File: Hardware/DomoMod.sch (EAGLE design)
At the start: 9 parts, among them Q1 BSS138, Q2 BSS138

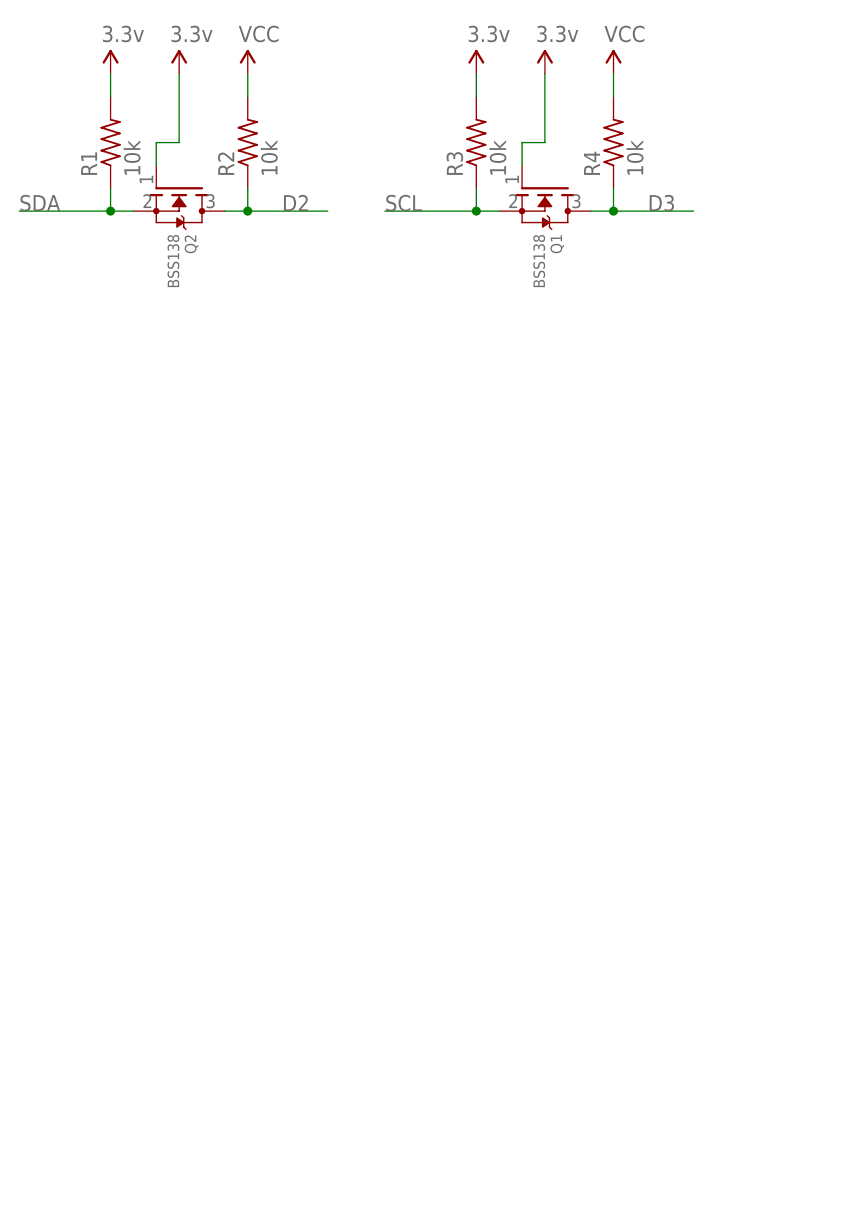
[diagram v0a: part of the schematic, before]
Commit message: Added schematics for Temp/Hum and barometric pressure sensor.
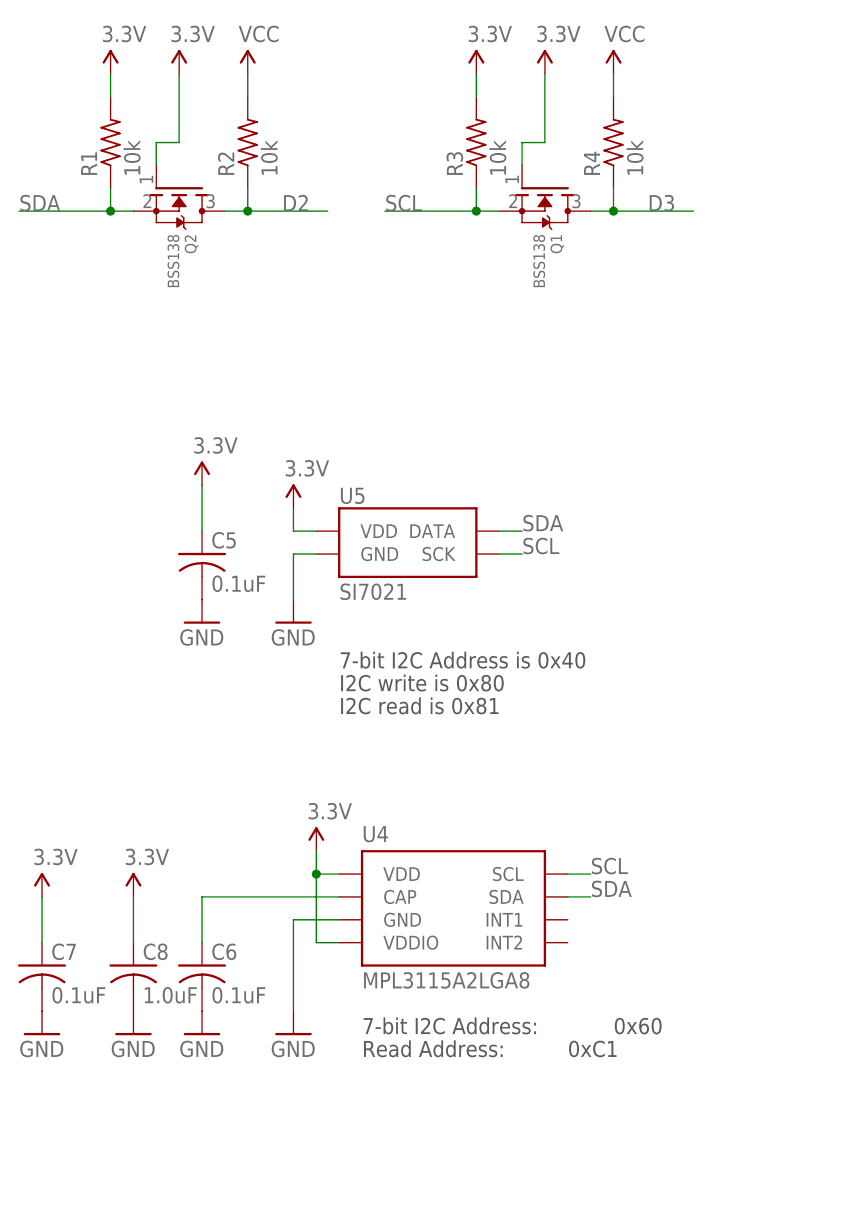
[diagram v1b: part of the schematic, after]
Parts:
- added C5, C6, C7: 0.1uF, resistor:C-USC0402
- added C8: 1.0uF, resistor:C-USC0402
- added U4: MPL3115A2LGA8, SparkFun-Sensors:MPL3115A2LGA8
- added U5: SI7021, SparkFun-Sensors:SI7021
- R1, R2, R3, R4: device resistor:R-US_R1206 -> resistor:R-US_R0402
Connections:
- new net N$5: C6.1, U4.CAP
- net 3.3V: now also C5.1, C7.1, C8.1, U4.VDD, U4.VDDIO, U5.VDD
- net GND: now also C5.2, C6.2, C7.2, C8.2, U4.GND, U5.GND
- net SCL: now also U4.SCL, U5.SCK
- net SDA: now also U4.SDA, U5.DATA
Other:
- note added: "0x60"
- note added: "0xC1"
- note added: "7-bit I2C Address is 0x40"
- note added: "7-bit I2C Address:"
- note added: "Humidity"
- note added: "I2C read is 0x81"
- note added: "I2C write is 0x80"
- note added: "Pressure"
- note added: "Read Address:"

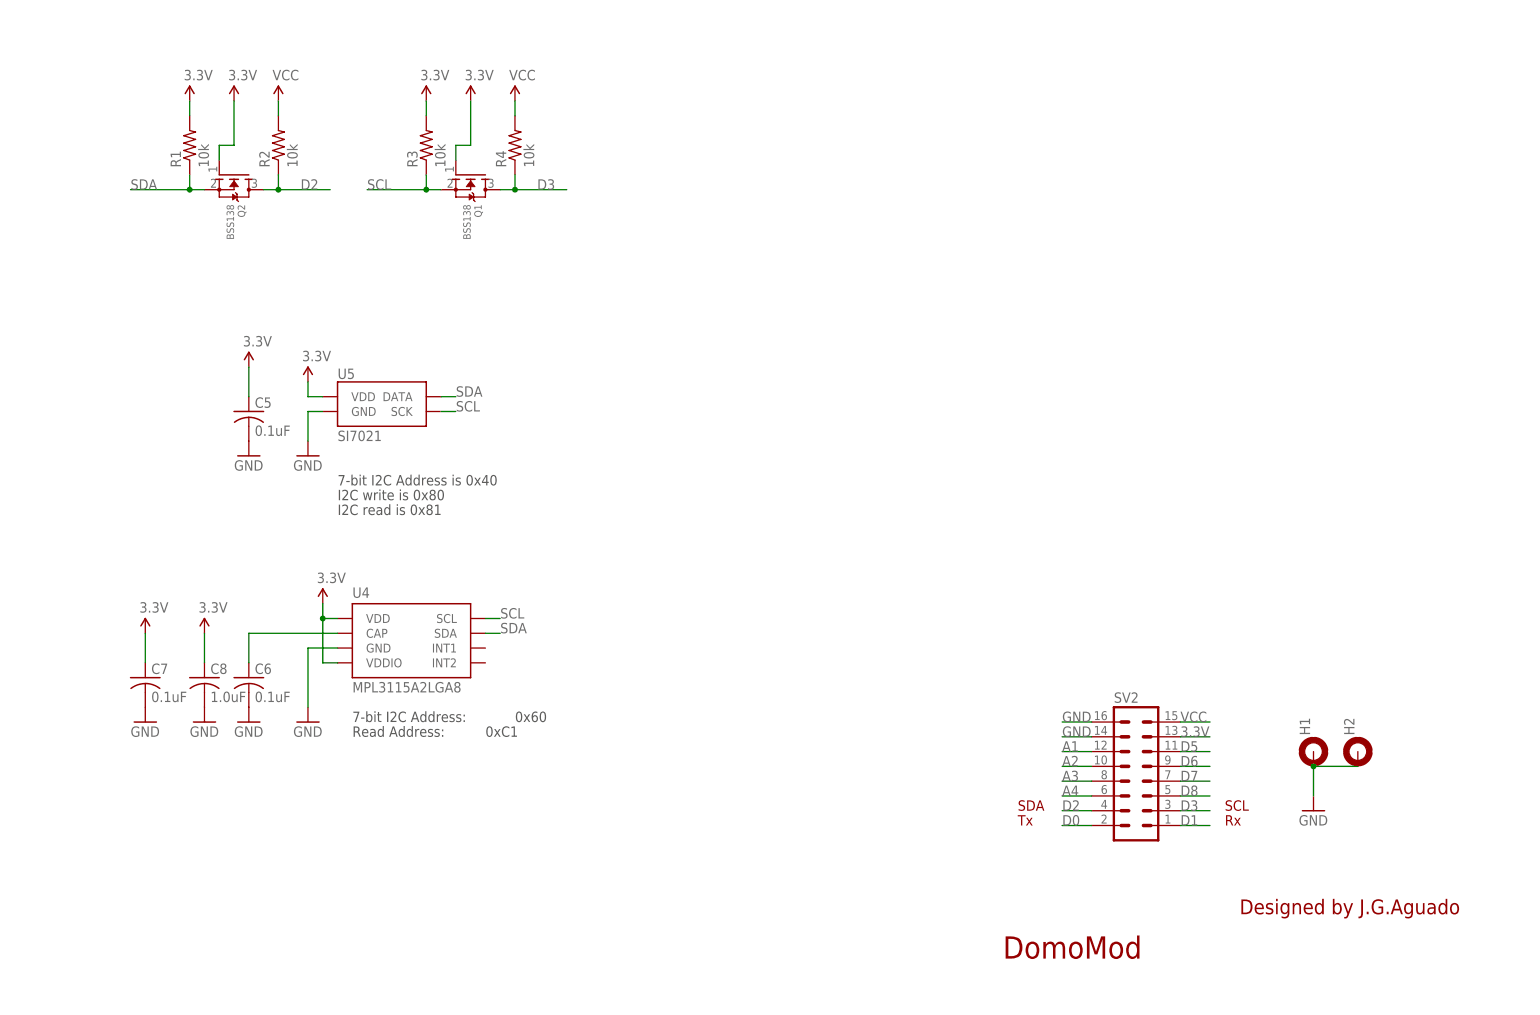
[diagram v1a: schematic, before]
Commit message: SCH: -Components placed and connected -Documented BRD: -Components placed -100% routed -DRC passed
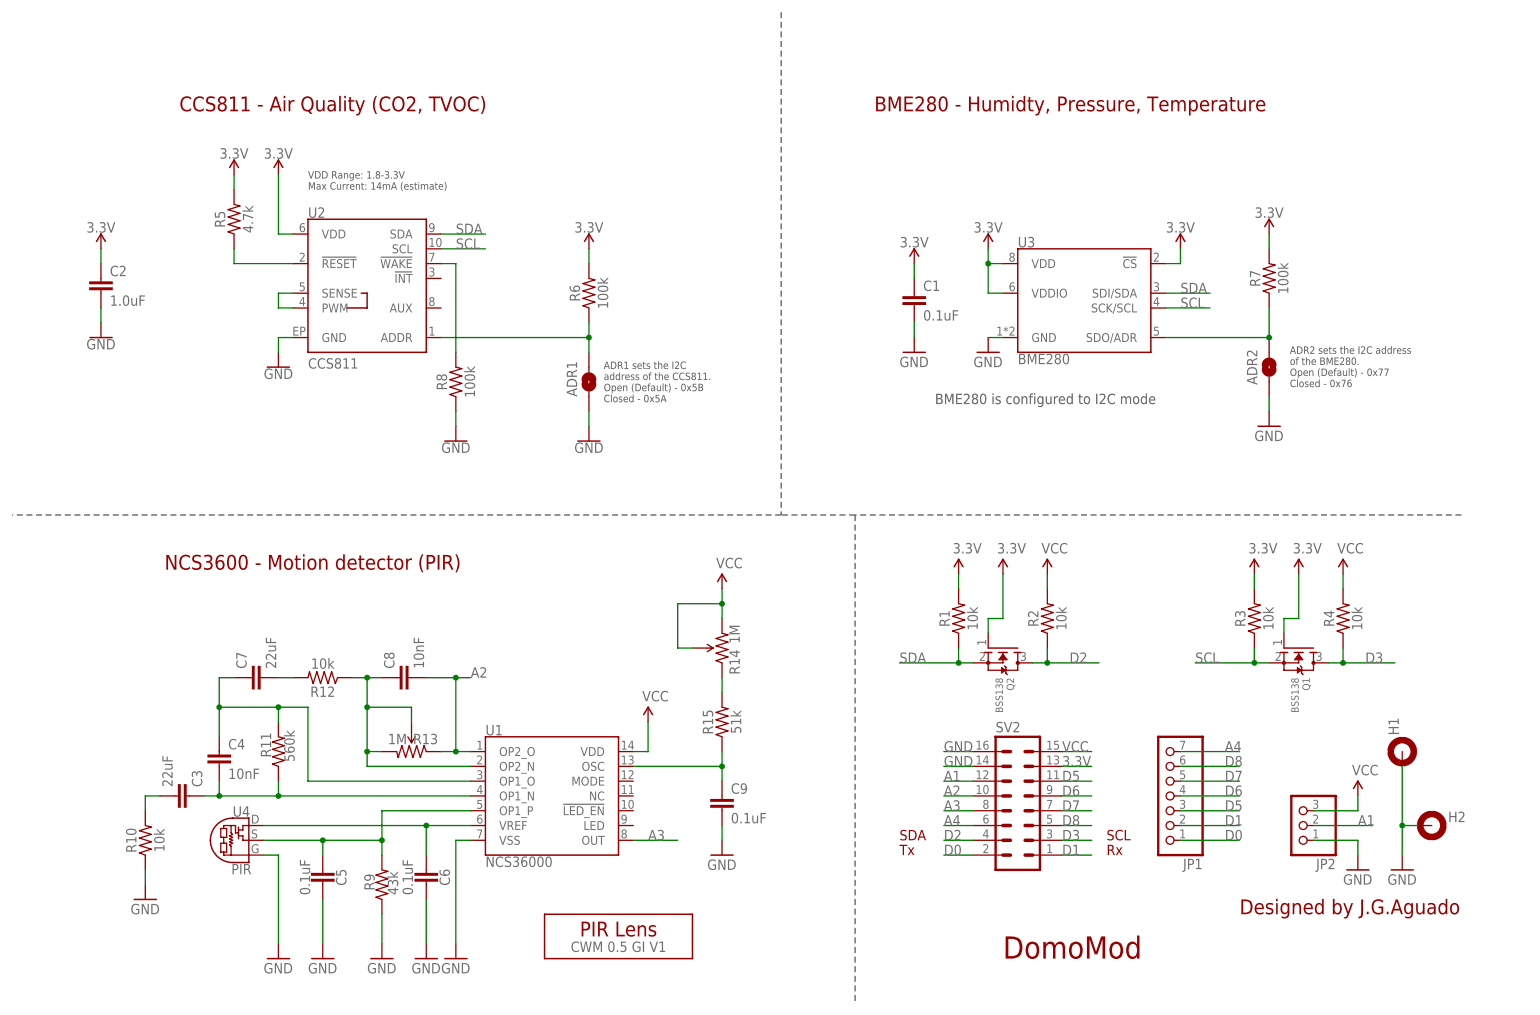
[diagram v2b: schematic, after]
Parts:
- removed U5: SI7021, SparkFun-Sensors:SI7021
- added ADR1, ADR2: JUMPER-SMT_2_NO_SILK, SparkFun-Jumpers:JUMPER-SMT_2_NO_SILK
- added C1, C9: 0.1uF, SparkFun-Capacitors:0.1UF-0603-25V-(+80/-20%)
- added C2: 1.0uF, SparkFun-Capacitors:1.0UF-0603-16V-10%
- added C3: 22uF, SparkFun-Capacitors:22UF-0805-6.3V-20%
- added C4: 10nF, SparkFun-Capacitors:10NF-0603-50V-10%
- added JP1: (no value), pinhead:PINHD-1X7/90
- added JP2: (no value), pinhead:PINHD-1X3
- added R10, R12: 10k, SparkFun-Resistors:10KOHM-0603-1/10W-1%
- added R11: 560k, openPIR-temp:560KOHM-0603-1/10W-5%
- added R13, R14: 1M, openPIR-temp:TRIMPOTTX33X-1M
- added R15: 51k, openPIR-temp:51KOHM-0603-1/10W-1%
- added R5: 4.7k, SparkFun-Resistors:4.7KOHM-0603-1/10W-1%
- added R6, R7, R8: 100k, SparkFun-Resistors:100KOHM-0603-1/10W-1%
- added R9: 43k, SparkFun-Resistors:43KOHM-0603-1/10W-1%
- added U$1: CWM 0.5 GI V1, openPIR-temp:PIR-LENSCWM-0.5-GI-V1
- added U1: NCS36000, openPIR-temp:NCS36000
- added U2: CCS811, SparkFun-Sensors:CCS811PRODUCTION
- added U3: BME280, SparkFun-Sensors:BME280
- C5, C6: device resistor:C-USC0402 -> SparkFun-Capacitors:0.1UF-0603-25V-(+80/-20%)
- C7: value 0.1uF -> 22uF; device resistor:C-USC0402 -> SparkFun-Capacitors:22UF-0805-6.3V-20%
- C8: value 1.0uF -> 10nF; device resistor:C-USC0402 -> SparkFun-Capacitors:10NF-0603-50V-10%
- R1, R2, R3, R4: device resistor:R-US_R0402 -> SparkFun-Resistors:100KOHM-0603-1/10W-1%
- U4: value MPL3115A2LGA8 -> PIR; device SparkFun-Sensors:MPL3115A2LGA8 -> openPIR-temp:PIR
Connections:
- new net !RST: R5.1, U2.!RESET!
- new net !WAKE: R8.2, U2.!WAKE!
- new net CCS811_ADDR: ADR1.2, R6.1, U2.ADDR
- new net N$1: C5.1, R9.2, U1.OP1_P, U4.S
- new net N$11: R14.CCW, R15.2
- new net N$2: C6.1, U1.VREF, U4.D
- new net N$3: C3.2, R10.2
- new net N$4: C7.2, R12.2
- new net N$6: C4.1, C7.1, R11.2, U1.OP1_O
- new net N$7: C8.1, R12.1, R13.CW, R13.WIPER, U1.OP2_N
- new net N$8: C9.1, R15.1, U1.OSC
- new net NTC_SENSE: U2.PWM, U2.SENSE
- new net SDO/ADR: ADR2.2, R7.1, U3.SDO/ADR
- net 3.3V: now also C1.1, C2.1, R5.2, R6.2, R7.2, U2.VDD, U3.!CS, U3.VDD, U3.VDDIO; no longer C5.1, C7.1, C8.1, U4.VDD, U4.VDDIO, U5.VDD
- net A1: now also JP2.2
- net A2: now also C8.2, R13.CCW, U1.OP2_O
- net A3: now also U1.OUT
- net A4: now also JP1.7
- net D0: now also JP1.1
- net D1: now also JP1.2
- net D5: now also JP1.3
- net D6: now also JP1.4
- net D7: now also JP1.5
- net D8: now also JP1.6
- net GND: now also ADR1.1, ADR2.1, C1.2, C2.2, C9.2, JP2.1, R10.1, R8.1, R9.1, U1.VSS, U2.GND, U3.GND, U4.G; no longer C7.2, C8.2, U4.GND, U5.GND
- net N$5: now also C3.1, C4.2, R11.1, U1.OP1_N; no longer C6.1, U4.CAP
- net SCL: now also U2.SCL, U3.SCK/SCL; no longer U4.SCL, U5.SCK
- net SDA: now also U2.SDA, U3.SDI/SDA; no longer U4.SDA, U5.DATA
- net VCC: now also JP2.3, R14.CW, R14.WIPER, U1.VDD
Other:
- note added: "ADR1 sets the I2C address of the CCS811. Open (Default) - 0x5B Closed - 0x5A"
- note added: "ADR2 sets the I2C address of the BME280. Open (Default) - 0x77 Closed - 0x76"
- note added: "BME280 - Humidty, Pressure, Temperature"
- note added: "BME280 is configured to I2C mode"
- note added: "CCS811 - Air Quality (CO2, TVOC)"
- note added: "NCS3600 - Motion detector (PIR)"
- note added: "VDD Range: 1.8-3.3V Max Current: 14mA (estimate)"
- note removed: "0x60"
- note removed: "0xC1"
- note removed: "7-bit I2C Address is 0x40"
- note removed: "7-bit I2C Address:"
- note removed: "I2C read is 0x81"
- note removed: "I2C write is 0x80"
- note removed: "Read Address:"
- moved on the sheet: C5, C6, C7, C8, H1, H2, Q1, Q2, R1, R2, R3, R4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

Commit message: Update
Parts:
- removed JP1: (no value), pinhead:PINHD-1X7/90
- removed JP2: (no value), pinhead:PINHD-1X3
- added JP3, JP4, JP5, JP6: (no value), pinhead:PINHD-1X2
- added JP7: (no value), pinhead:PINHD-1X3
- added JP8: (no value), pinhead:PINHD-1X4
- added R16: 1k, SparkFun-Resistors:100KOHM-0603-1/10W-1%
- added R17, R18, R19: 10k, SparkFun-Resistors:100KOHM-0603-1/10W-1%
- added T1: MMBT2222A, transistor:BC808-NPN-SOT23-BEC
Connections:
- new net N$10: R16.1, T1.B
- new net N$9: JP3.2, T1.C
- net A1: now also JP4.2, R17.2; no longer JP2.2
- net A3: now also JP6.2, R19.2; no longer U1.OUT
- net A4: now also JP5.2, R18.2; no longer JP1.7
- net D0: no longer JP1.1
- net D1: no longer JP1.2
- net D2: now also JP8.2
- net D3: now also JP8.1
- net D5: now also JP7.1; no longer JP1.3
- net D6: now also R16.2; no longer JP1.4
- net D7: now also JP6.1; no longer JP1.5
- net D8: now also U1.OUT; no longer JP1.6
- net GND: now also JP7.3, JP8.4, R17.1, R18.1, R19.1, T1.E; no longer JP2.1
- net N$4: now also R12.1; no longer R12.2
- net N$5: now also C4.1; no longer C4.2
- net N$6: now also C4.2; no longer C4.1
- net N$7: now also R12.2; no longer R12.1
- net VCC: now also JP3.1, JP4.1, JP5.1, JP7.2, JP8.3; no longer JP2.3
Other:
- note added: "External connectors"
- moved on the sheet: ADR2, C1, C4, Q1, Q2, R1, R12, R2, R3, R4, R7, U3

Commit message: Update
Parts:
- removed JP7: (no value), pinhead:PINHD-1X3
- removed JP8: (no value), pinhead:PINHD-1X4
- removed R18, R19: 10k, SparkFun-Resistors:100KOHM-0603-1/10W-1%
- added JP1, JP2: (no value), pinhead:PINHD-1X2
- added POT1, POT2: 1M, openPIR-temp:TRIMPOTTX33X-1M
- JP5: device pinhead:PINHD-1X2 -> pinhead:PINHD-1X3
- JP6: device pinhead:PINHD-1X2 -> pinhead:PINHD-1X4
- R1: value 10k -> 1k
- R11: value 560k -> 10k; device openPIR-temp:560KOHM-0603-1/10W-5% -> SparkFun-Resistors:10KOHM-0603-1/10W-1%
- R12: value 10k -> 43k; device SparkFun-Resistors:10KOHM-0603-1/10W-1% -> SparkFun-Resistors:43KOHM-0603-1/10W-1%
- R13: value 1M -> 51k; device openPIR-temp:TRIMPOTTX33X-1M -> openPIR-temp:51KOHM-0603-1/10W-1%
- R14: value 1M -> 100k; device openPIR-temp:TRIMPOTTX33X-1M -> SparkFun-Resistors:100KOHM-0603-1/10W-1%
- R15: value 51k -> 100k; device openPIR-temp:51KOHM-0603-1/10W-1% -> SparkFun-Resistors:100KOHM-0603-1/10W-1%
- R16: value 1k -> 100k
- R17: value 10k -> 560k; device SparkFun-Resistors:100KOHM-0603-1/10W-1% -> openPIR-temp:560KOHM-0603-1/10W-5%
- R2: value 10k -> 4.7k; device SparkFun-Resistors:100KOHM-0603-1/10W-1% -> SparkFun-Resistors:4.7KOHM-0603-1/10W-1%
- R5: value 4.7k -> 10k; device SparkFun-Resistors:4.7KOHM-0603-1/10W-1% -> SparkFun-Resistors:100KOHM-0603-1/10W-1%
- R6, R7, R8: value 100k -> 10k
- R9: value 43k -> 10k; device SparkFun-Resistors:43KOHM-0603-1/10W-1% -> SparkFun-Resistors:100KOHM-0603-1/10W-1%
- renumbered SV2 to SV1
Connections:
- net !RST: now also R2.1; no longer R5.1
- net !WAKE: now also R14.2; no longer R8.2
- net 3.3V: now also R15.2, R16.2, R2.2; no longer R1.2, R6.2, R7.2
- net A1: now also JP2.2, R7.2; no longer JP4.2, R17.2
- net A2: now also POT1.CCW; no longer R13.CCW
- net A3: now also JP4.2, R9.2; no longer JP6.2, R19.2
- net A4: now also JP3.2, R8.2; no longer JP5.2, R18.2
- net CCS811_ADDR: now also R15.1; no longer R6.1
- net D2: now also JP6.2, R4.1; no longer JP8.2, R2.1
- net D3: now also JP6.1, R6.1; no longer JP8.1, R4.1
- net D5: now also JP5.1; no longer JP7.1
- net D6: now also R1.2; no longer R16.2
- net D7: now also JP4.1; no longer JP6.1
- net GND: now also JP5.3, JP6.4, R12.1, R14.1, R7.1; no longer JP7.3, JP8.4, R17.1, R18.1, R19.1
- net N$1: now also R12.2; no longer R9.2
- net N$10: now also R1.1; no longer R16.1
- net N$11: now also POT2.CCW, R13.2; no longer R14.CCW, R15.2
- net N$4: now also R11.1; no longer R12.1
- net N$5: now also R17.1; no longer R11.1
- net N$6: now also R17.2; no longer R11.2
- net N$7: now also POT1.CW, POT1.WIPER, R11.2; no longer R12.2, R13.CW, R13.WIPER
- net N$8: now also R13.1; no longer R15.1
- net N$9: now also JP1.2; no longer JP3.2
- net SCL: now also R5.1; no longer R3.1
- net SDA: now also R3.1; no longer R1.1
- net SDO/ADR: now also R16.1; no longer R7.1
- net VCC: now also JP1.1, JP2.1, JP5.2, JP6.3, POT2.CW, POT2.WIPER, R6.2; no longer JP4.1, JP5.1, JP7.2, JP8.3, R14.CW, R14.WIPER, R2.2
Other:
- moved on the sheet: JP3, JP4, R1, R11, R12, R15, R16, R17, R2, R3, R4, R5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
